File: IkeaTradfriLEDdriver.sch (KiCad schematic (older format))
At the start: 9 parts, among them J1 input, J2 PWM, J3 LED strip, Q1 BUZ11, U1 LM741

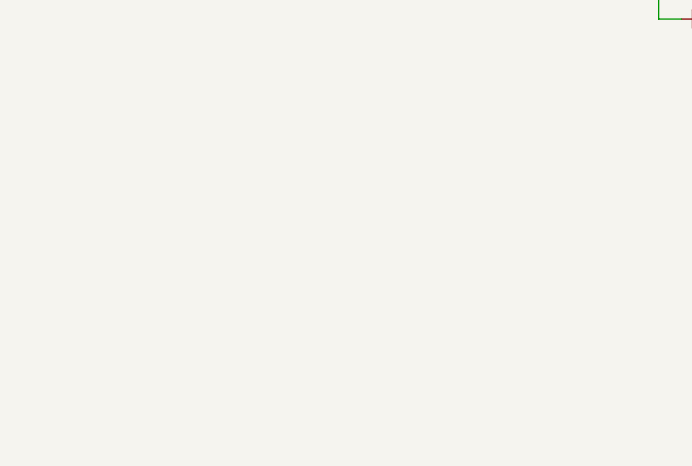
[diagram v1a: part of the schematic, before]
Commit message: Pridany regulator lm1117 z 12V na 3.3V
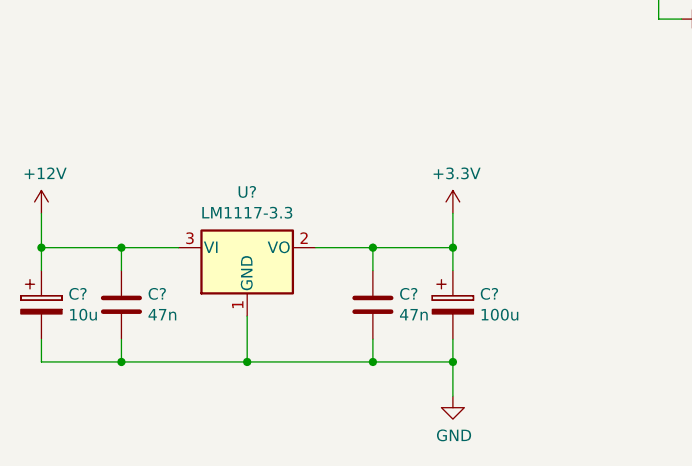
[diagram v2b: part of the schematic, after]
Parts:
- added C? (x2): 47n, symbol Device:C
- added C?: 10u, symbol Device:CP
- added C?: 100u, symbol Device:CP
- added U?: LM1117-3.3, symbol Regulator_Linear:LM1117-3.3
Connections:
- net +12V: now also C?.1, C?.1, U?.3 (VI)
- net GND: now also C?.2, C?.2, C?.2, C?.2, U?.1 (GND)
- new net +3V3: C?.1, C?.1, U?.2 (VO)
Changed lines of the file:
@@
 	-1   0    0    1
 $EndComp
+$Comp
+L Regulator_Linear:LM1117-3.3 U?
+U 1 1 5C75B3A7
+P 1950 4500
+F 0 "U?" H 1950 4742 50  0000 C CNN
+F 1 "LM1117-3.3" H 1950 4651 50  0000 C CNN
+F 2 "" H 1950 4500 50  0001 C CNN
+F 3 "http://www.ti.com/lit/ds/symlink/lm1117.pdf" H 1950 4500 50  0001 C CNN
+	1    1950 4500
+	1    0    0    -1
+$EndComp
+$Comp
+L power:+12V #PWR?
+U 1 1 5C75B47A
+P 1050 4350
+F 0 "#PWR?" H 1050 4200 50  0001 C CNN
+F 1 "+12V" H 1065 4523 50  0000 C CNN
+F 2 "" H 1050 4350 50  0001 C CNN
+F 3 "" H 1050 4350 50  0001 C CNN
+	1    1050 4350
+	1    0    0    -1
+$EndComp
+$Comp
+L power:+3.3V #PWR?
+U 1 1 5C75B500
+P 2850 4350
+F 0 "#PWR?" H 2850 4200 50  0001 C CNN
+F 1 "+3.3V" H 2865 4523 50  0000 C CNN
+F 2 "" H 2850 4350 50  0001 C CNN
+F 3 "" H 2850 4350 50  0001 C CNN
+	1    2850 4350
+	1    0    0    -1
+$EndComp
+$Comp
+L Device:C C?
+U 1 1 5C75B55C
+P 1400 4750
+F 0 "C?" H 1515 4796 50  0000 L CNN
+F 1 "47n" H 1515 4705 50  0000 L CNN
+F 2 "" H 1438 4600 50  0001 C CNN
+F 3 "~" H 1400 4750 50  0001 C CNN
+	1    1400 4750
+	1    0    0    -1
+$EndComp
+$Comp
+L Device:C C?
+U 1 1 5C75B5D1
+P 2500 4750
+F 0 "C?" H 2615 4796 50  0000 L CNN
+F 1 "47n" H 2615 4705 50  0000 L CNN
+F 2 "" H 2538 4600 50  0001 C CNN
+F 3 "~" H 2500 4750 50  0001 C CNN
+	1    2500 4750
+	1    0    0    -1
+$EndComp
+$Comp
+L Device:CP C?
+U 1 1 5C75B961
+P 1050 4750
+F 0 "C?" H 1168 4796 50  0000 L CNN
+F 1 "10u" H 1168 4705 50  0000 L CNN
+F 2 "" H 1088 4600 50  0001 C CNN
+F 3 "~" H 1050 4750 50  0001 C CNN
+	1    1050 4750
+	1    0    0    -1
+$EndComp
+$Comp
+L Device:CP C?
+U 1 1 5C75BADC
+P 2850 4750
+F 0 "C?" H 2968 4796 50  0000 L CNN
+F 1 "100u" H 2968 4705 50  0000 L CNN
+F 2 "" H 2888 4600 50  0001 C CNN
+F 3 "~" H 2850 4750 50  0001 C CNN
+	1    2850 4750
+	1    0    0    -1
+$EndComp
+Wire Wire Line
+	1050 4350 1050 4500
+Wire Wire Line
+	1400 4600 1400 4500
+Wire Wire Line
+	1400 4500 1050 4500
+Connection ~ 1050 4500
+Wire Wire Line
+	1050 4500 1050 4600
+Wire Wire Line
+	1400 4500 1650 4500
+Connection ~ 1400 4500
+Wire Wire Line
+	2250 4500 2500 4500
+Wire Wire Line
+	2500 4500 2500 4600
+Wire Wire Line
+	2500 4500 2850 4500
+Wire Wire Line
+	2850 4500 2850 4600
+Connection ~ 2500 4500
+Wire Wire Line
+	2850 4500 2850 4350
+Connection ~ 2850 4500
+Wire Wire Line
+	1050 4900 1050 5000
+Wire Wire Line
+	1050 5000 1400 5000
+Wire Wire Line
+	2850 5000 2850 4900
+Wire Wire Line
+	2500 4900 2500 5000
+Connection ~ 2500 5000
+Wire Wire Line
+	2500 5000 2850 5000
+Wire Wire Line
+	1950 4800 1950 5000
+Connection ~ 1950 5000
+Wire Wire Line
+	1950 5000 2500 5000
+Wire Wire Line
+	1400 4900 1400 5000
+Connection ~ 1400 5000
+Wire Wire Line
+	1400 5000 1950 5000
+$Comp
+L power:GND #PWR?
+U 1 1 5C75EF0F
+P 2850 5150
+F 0 "#PWR?" H 2850 4900 50  0001 C CNN
+F 1 "GND" H 2855 4977 50  0000 C CNN
+F 2 "" H 2850 5150 50  0001 C CNN
+F 3 "" H 2850 5150 50  0001 C CNN
+	1    2850 5150
+	1    0    0    -1
+$EndComp
+Wire Wire Line
+	2850 5000 2850 5150
+Connection ~ 2850 5000
 $EndSCHEMATC

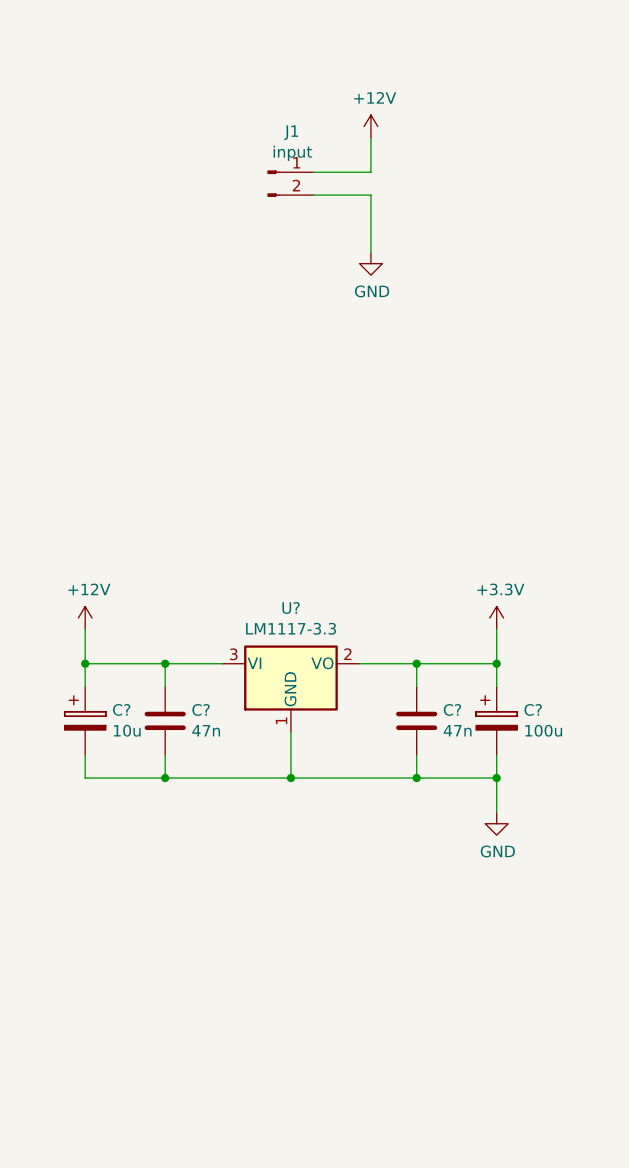
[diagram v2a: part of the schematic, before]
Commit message: Pinheader pro Ikea zigbit module
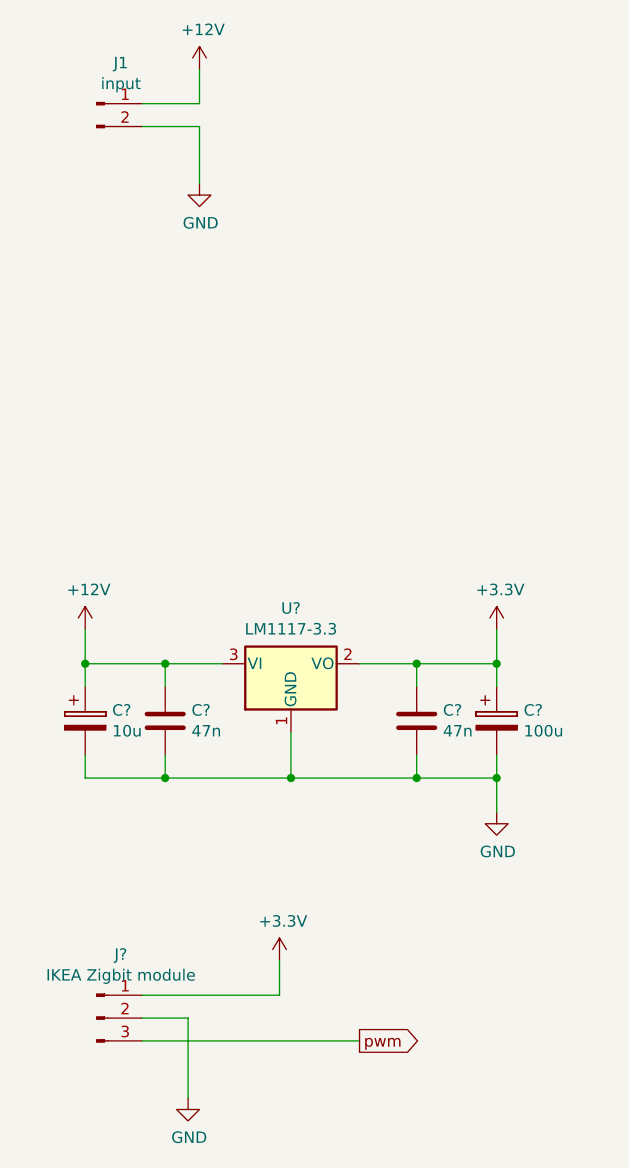
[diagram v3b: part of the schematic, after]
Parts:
- added J?: IKEA Zigbit module, Connector_PinHeader_1.27mm:PinHeader_1x03_P1.27mm_Vertical, symbol Connector:Conn_01x03_Male
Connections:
- net +3V3: now also J?.1 (Pin_1)
- net GND: now also J?.2 (Pin_2)
- new net pwm: J?.3 (Pin_3)
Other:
- moved on the sheet: J1
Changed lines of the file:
@@
 L Connector:Conn_01x02_Male J1
 U 1 1 5C6C6F0A
-P 1850 2350
-F 0 "J1" H 1956 2528 50  0000 C CNN
-F 1 "input" H 1956 2437 50  0000 C CNN
-F 2 "Connector_Wire:SolderWirePad_1x02_P5.08mm_Drill1.5mm" H 1850 2350 50  0001 C CNN
-F 3 "~" H 1850 2350 50  0001 C CNN
-	1    1850 2350
+P 1100 2050
+F 0 "J1" H 1206 2228 50  0000 C CNN
+F 1 "input" H 1206 2137 50  0000 C CNN
+F 2 "Connector_Wire:SolderWirePad_1x02_P5.08mm_Drill1.5mm" H 1100 2050 50  0001 C CNN
+F 3 "~" H 1100 2050 50  0001 C CNN
+	1    1100 2050
 	1    0    0    -1
 $EndComp
@@
 L power:+12V #PWR0102
 U 1 1 5C7538CD
-P 2300 2200
-F 0 "#PWR0102" H 2300 2050 50  0001 C CNN
-F 1 "+12V" H 2315 2373 50  0000 C CNN
-F 2 "" H 2300 2200 50  0001 C CNN
-F 3 "" H 2300 2200 50  0001 C CNN
-	1    2300 2200
-	1    0    0    -1
-$EndComp
-Wire Wire Line
-	2300 2200 2300 2350
-Wire Wire Line
-	2300 2350 2050 2350
-Wire Wire Line
-	2050 2450 2300 2450
-Wire Wire Line
-	2300 2450 2300 2700
+P 1550 1900
+F 0 "#PWR0102" H 1550 1750 50  0001 C CNN
+F 1 "+12V" H 1565 2073 50  0000 C CNN
+F 2 "" H 1550 1900 50  0001 C CNN
+F 3 "" H 1550 1900 50  0001 C CNN
+	1    1550 1900
+	1    0    0    -1
+$EndComp
+Wire Wire Line
+	1550 1900 1550 2050
+Wire Wire Line
+	1550 2050 1300 2050
+Wire Wire Line
+	1300 2150 1550 2150
+Wire Wire Line
+	1550 2150 1550 2400
 $Comp
 L power:GND #PWR0106
 U 1 1 5C753C9C
-P 2300 2700
-F 0 "#PWR0106" H 2300 2450 50  0001 C CNN
-F 1 "GND" H 2305 2527 50  0000 C CNN
-F 2 "" H 2300 2700 50  0001 C CNN
-F 3 "" H 2300 2700 50  0001 C CNN
-	1    2300 2700
+P 1550 2400
+F 0 "#PWR0106" H 1550 2150 50  0001 C CNN
+F 1 "GND" H 1555 2227 50  0000 C CNN
+F 2 "" H 1550 2400 50  0001 C CNN
+F 3 "" H 1550 2400 50  0001 C CNN
+	1    1550 2400
 	1    0    0    -1
 $EndComp
@@
 	2850 5000 2850 5150
 Connection ~ 2850 5000
+$Comp
+L Connector:Conn_01x03_Male J?
+U 1 1 5C761CEC
+P 1100 6050
+F 0 "J?" H 1206 6328 50  0000 C CNN
+F 1 "IKEA Zigbit module" H 1206 6237 50  0000 C CNN
+F 2 "Connector_PinHeader_1.27mm:PinHeader_1x03_P1.27mm_Vertical" H 1100 6050 50  0001 C CNN
+F 3 "~" H 1100 6050 50  0001 C CNN
+	1    1100 6050
+	1    0    0    -1
+$EndComp
+$Comp
+L power:GND #PWR?
+U 1 1 5C76258E
+P 1500 6400
+F 0 "#PWR?" H 1500 6150 50  0001 C CNN
+F 1 "GND" H 1505 6227 50  0000 C CNN
+F 2 "" H 1500 6400 50  0001 C CNN
+F 3 "" H 1500 6400 50  0001 C CNN
+	1    1500 6400
+	1    0    0    -1
+$EndComp
+$Comp
+L power:+3.3V #PWR?
+U 1 1 5C762623
+P 1900 5800
+F 0 "#PWR?" H 1900 5650 50  0001 C CNN
+F 1 "+3.3V" H 1915 5973 50  0000 C CNN
+F 2 "" H 1900 5800 50  0001 C CNN
+F 3 "" H 1900 5800 50  0001 C CNN
+	1    1900 5800
+	1    0    0    -1
+$EndComp
+Text GLabel 2250 6150 2    50   Output ~ 0
+pwm
+Wire Wire Line
+	1300 5950 1900 5950
+Wire Wire Line
+	1900 5950 1900 5800
+Wire Wire Line
+	1300 6050 1500 6050
+Wire Wire Line
+	1500 6050 1500 6400
+Wire Wire Line
+	1300 6150 2250 6150
 $EndSCHEMATC
